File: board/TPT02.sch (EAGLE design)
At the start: 20 parts, among them SW4 SW_SLIDECUS12, U1 MOD_CYBLE022001-00, U2 REG_LTC1502

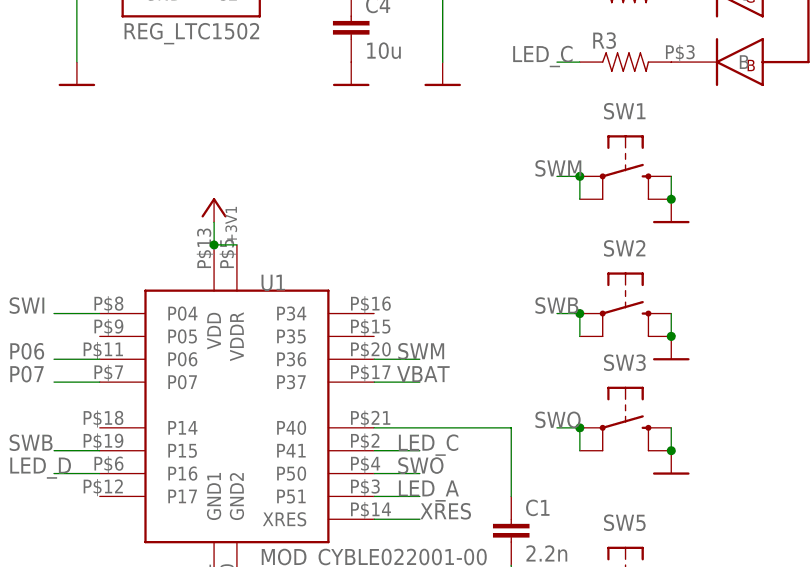
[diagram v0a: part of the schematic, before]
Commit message: 基板の修正（バッテリ電圧計測＆TXD端子）
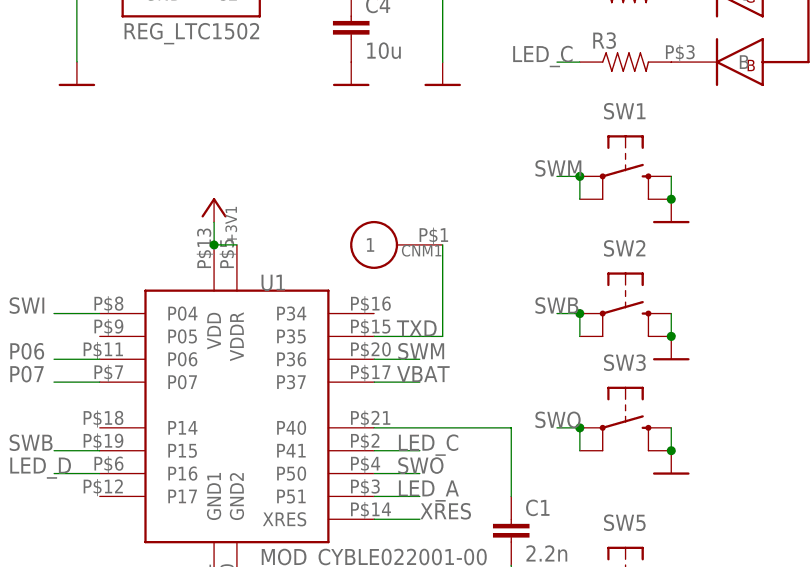
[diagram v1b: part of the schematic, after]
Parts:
- added CNM1: CON_P01SMD1MM, akita:CON_P01SMD1MM
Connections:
- new net TXD: CNM1.1, U1.P35
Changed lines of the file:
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@@
 <part name="SW5" library="akita" deviceset="SW_TACT" device="EVQPU02"/>
 <part name="GND10" library="akita" deviceset="POW_GND" device=""/>
+<part name="CNM1" library="akita" deviceset="CON_P01" device="SMD1MM"/>
 </parts>
 <sheets>
@@
 <instance part="SW5" gate="1" x="99.06" y="22.86" rot="R270"/>
 <instance part="GND10" gate="1" x="104.14" y="17.78"/>
+<instance part="CNM1" gate="G$1" x="71.12" y="60.96" rot="R180"/>
 </instances>
 <busses>
@@
 </segment>
 </net>
+<net name="TXD" class="0">
+<segment>
+<pinref part="U1" gate="G$1" pin="P35"/>
+<wire x1="71.12" y1="50.8" x2="78.74" y2="50.8" width="0.1524" layer="91"/>
+<label x="73.66" y="50.8" size="1.778" layer="95"/>
+<pinref part="CNM1" gate="G$1" pin="1"/>
+<wire x1="78.74" y1="50.8" x2="78.74" y2="60.96" width="0.1524" layer="91"/>
+</segment>
+</net>

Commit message: 両脇のスイッチ(SWB/SWO)のパッケージを変更
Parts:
- SW2, SW3: device akita:SW_TACTTSKA2J -> akita:SW_TACTPTS525SK08
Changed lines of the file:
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@@
 <grid distance="0.1" unitdist="inch" unit="inch" style="lines" multiple="1" display="no" altdistance="0.01" altunitdist="inch" altunit="inch"/>
 <layers>
-<layer number="1" name="Top" color="4" fill="1" visible="no" active="no"/>
-<layer number="16" name="Bottom" color="1" fill="1" visible="no" active="no"/>
-<layer number="17" name="Pads" color="2" fill="1" visible="no" active="no"/>
-<layer number="18" name="Vias" color="2" fill="1" visible="no" active="no"/>
-<layer number="19" name="Unrouted" color="6" fill="1" visible="no" active="no"/>
-<layer number="20" name="Dimension" color="15" fill="1" visible="no" active="no"/>
-<layer number="21" name="tPlace" color="7" fill="1" visible="no" active="no"/>
-<layer number="22" name="bPlace" color="7" fill="1" visible="no" active="no"/>
-<layer number="23" name="tOrigins" color="15" fill="1" visible="no" active="no"/>
-<layer number="24" name="bOrigins" color="15" fill="1" visible="no" active="no"/>
-<layer number="25" name="tNames" color="7" fill="1" visible="no" active="no"/>
-<layer number="26" name="bNames" color="7" fill="1" visible="no" active="no"/>
-<layer number="27" name="tValues" color="7" fill="1" visible="no" active="no"/>
-<layer number="28" name="bValues" color="7" fill="1" visible="no" active="no"/>
+<layer number="1" name="Top" color="4" fill="1" visible="yes" active="no"/>
+<layer number="16" name="Bottom" color="1" fill="1" visible="yes" active="no"/>
+<layer number="17" name="Pads" color="2" fill="1" visible="yes" active="no"/>
+<layer number="18" name="Vias" color="2" fill="1" visible="yes" active="no"/>
+<layer number="19" name="Unrouted" color="6" fill="1" visible="yes" active="no"/>
+<layer number="20" name="Dimension" color="15" fill="1" visible="yes" active="no"/>
+<layer number="21" name="tPlace" color="7" fill="1" visible="yes" active="no"/>
+<layer number="22" name="bPlace" color="7" fill="1" visible="yes" active="no"/>
+<layer number="23" name="tOrigins" color="15" fill="1" visible="yes" active="no"/>
+<layer number="24" name="bOrigins" color="15" fill="1" visible="yes" active="no"/>
+<layer number="25" name="tNames" color="7" fill="1" visible="yes" active="no"/>
+<layer number="26" name="bNames" color="7" fill="1" visible="yes" active="no"/>
+<layer number="27" name="tValues" color="7" fill="1" visible="yes" active="no"/>
+<layer number="28" name="bValues" color="7" fill="1" visible="yes" active="no"/>
 <layer number="29" name="tStop" color="7" fill="3" visible="no" active="no"/>
 <layer number="30" name="bStop" color="7" fill="6" visible="no" active="no"/>
@@
 <layer number="35" name="tGlue" color="7" fill="4" visible="no" active="no"/>
 <layer number="36" name="bGlue" color="7" fill="5" visible="no" active="no"/>
-<layer number="37" name="tTest" color="7" fill="1" visible="no" active="no"/>
-<layer number="38" name="bTest" color="7" fill="1" visible="no" active="no"/>
+<layer number="37" name="tTest" color="7" fill="1" visible="yes" active="no"/>
+<layer number="38" name="bTest" color="7" fill="1" visible="yes" active="no"/>
 <layer number="39" name="tKeepout" color="4" fill="11" visible="no" active="no"/>
 <layer number="40" name="bKeepout" color="1" fill="11" visible="no" active="no"/>
@@
 <layer number="44" name="Drills" color="7" fill="1" visible="no" active="no"/>
 <layer number="45" name="Holes" color="7" fill="1" visible="no" active="no"/>
-<layer number="46" name="Milling" color="3" fill="1" visible="no" active="no"/>
-<layer number="47" name="Measures" color="7" fill="1" visible="no" active="no"/>
-<layer number="48" name="Document" color="7" fill="1" visible="no" active="no"/>
-<layer number="49" name="Reference" color="7" fill="1" visible="no" active="no"/>
-<layer number="50" name="dxf" color="7" fill="1" visible="no" active="no"/>
-<layer number="51" name="tDocu" color="7" fill="1" visible="no" active="no"/>
-<layer number="52" name="bDocu" color="7" fill="1" visible="no" active="no"/>
-<layer number="53" name="tGND_GNDA" color="7" fill="9" visible="no" active="no"/>
-<layer number="54" name="bGND_GNDA" color="1" fill="9" visible="no" active="no"/>
-<layer number="56" name="wert" color="7" fill="1" visible="no" active="no"/>
-<layer number="57" name="tCAD" color="7" fill="1" visible="no" active="no"/>
-<layer number="59" name="Invisible" color="7" fill="1" visible="no" active="no"/>
-<layer number="61" name="stand" color="7" fill="1" visible="no" active="no"/>
+<layer number="46" name="Milling" color="3" fill="1" visible="yes" active="no"/>
+<layer number="47" name="Measures" color="7" fill="1" visible="yes" active="no"/>
+<layer number="48" name="Document" color="7" fill="1" visible="yes" active="no"/>
+<layer number="49" name="Reference" color="7" fill="1" visible="yes" active="no"/>
+<layer number="50" name="dxf" color="7" fill="1" visible="yes" active="no"/>
+<layer number="51" name="tDocu" color="7" fill="1" visible="yes" active="no"/>
+<layer number="52" name="bDocu" color="7" fill="1" visible="yes" active="no"/>
+<layer number="53" name="tGND_GNDA" color="7" fill="9" visible="yes" active="no"/>
+<layer number="54" name="bGND_GNDA" color="1" fill="9" visible="yes" active="no"/>
+<layer number="56" name="wert" color="7" fill="1" visible="yes" active="no"/>
+<layer number="57" name="tCAD" color="7" fill="1" visible="yes" active="no"/>
+<layer number="59" name="Invisible" color="7" fill="1" visible="yes" active="no"/>
+<layer number="61" name="stand" color="7" fill="1" visible="yes" active="no"/>
 <layer number="90" name="Modules" color="5" fill="1" visible="yes" active="yes"/>
 <layer number="91" name="Nets" color="2" fill="1" visible="yes" active="yes"/>
@@
 <part name="CNM" library="akita" deviceset="CON_P01" device="SMD1MM"/>
 <part name="SW1" library="akita" deviceset="SW_TACT" device="EVQP2"/>
-<part name="SW3" library="akita" deviceset="SW_TACT" device="TSKA2J"/>
-<part name="SW2" library="akita" deviceset="SW_TACT" device="TSKA2J"/>
+<part name="SW3" library="akita" deviceset="SW_TACT" device="PTS525SK08"/>
+<part name="SW2" library="akita" deviceset="SW_TACT" device="PTS525SK08"/>
 <part name="SW4" library="akita" deviceset="SW_SLIDE" device="CUS12"/>
 <part name="D1" library="akita" deviceset="LED_RGB_OSTB0603C1C" device=""/>
